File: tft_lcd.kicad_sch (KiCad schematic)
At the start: 4 parts, among them J1 Left_02x24, J2 Right Header, J3 Right_02x24, J4 Left Header

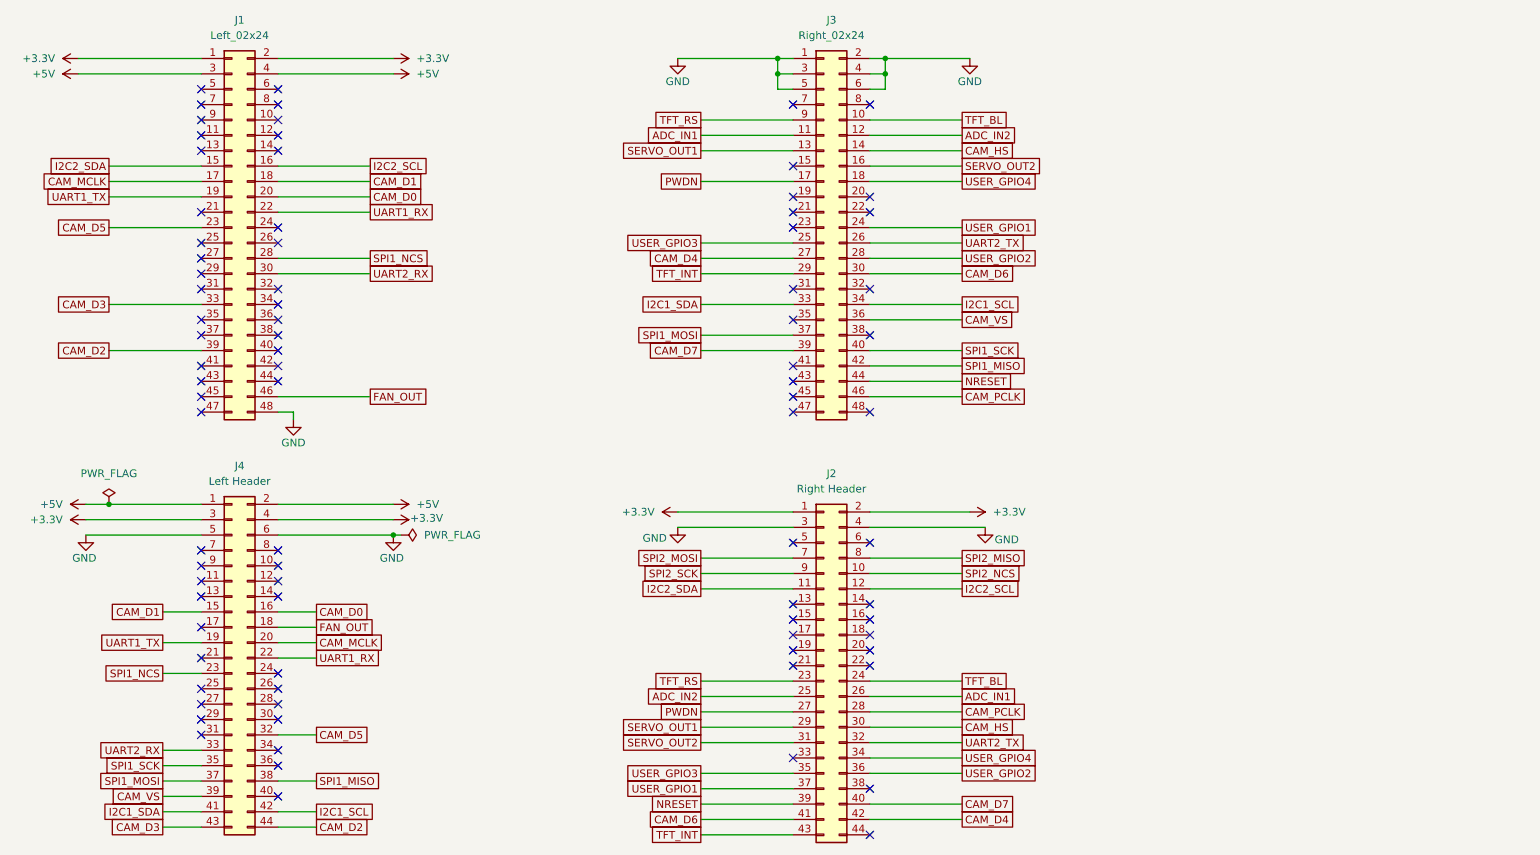
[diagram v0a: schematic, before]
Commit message: completed part placement
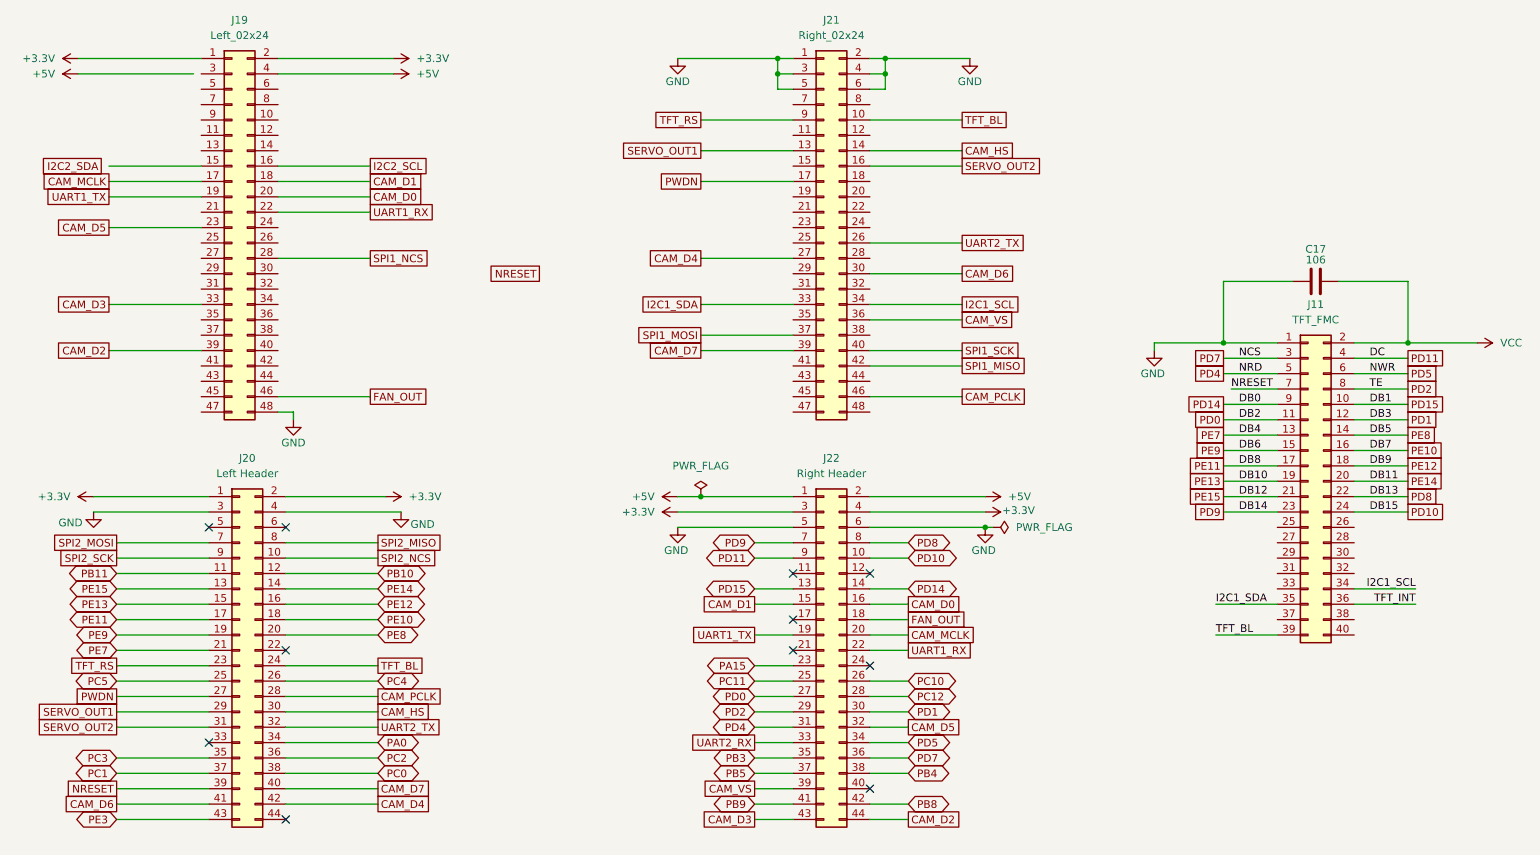
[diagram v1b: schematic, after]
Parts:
- added C17: 106, Capacitor_SMD:C_0805_2012Metric_Pad1.18x1.45mm_HandSolder, symbol LM2676S-3.3_NOPB:C
- added J11: TFT_FMC, Connector_PinHeader_2.54mm:PinHeader_2x20_P2.54mm_Vertical, symbol LM2676S-3.3_NOPB:Conn_02x20_Odd_Even
- J19: renamed from J1; footprint Connector_PinHeader_2.54mm:PinHeader_2x24_P2.54mm_Vertical -> (none)
- J20: renamed from J2; value Right Header -> Left Header
- J21: renamed from J3; footprint Connector_PinHeader_2.54mm:PinHeader_2x24_P2.54mm_Vertical -> (none)
- J22: renamed from J4; value Left Header -> Right Header
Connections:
- net +5V: no longer J19.3 (Pin_3)
- net GND: now also C17.1, J11.1 (Pin_1)
- net I2C1_SCL: now also J11.34 (Pin_34); no longer J22.42 (Pin_42)
- net I2C1_SDA: now also J11.35 (Pin_35); no longer J22.41 (Pin_41)
- net I2C2_SCL: no longer J20.12 (Pin_12)
- net I2C2_SDA: no longer J19.15 (Pin_15), J20.11 (Pin_11)
- net NRESET: now also J11.7 (Pin_7); no longer J21.44 (Pin_44)
- net SPI1_MISO: no longer J22.38 (Pin_38)
- net SPI1_MOSI: no longer J22.37 (Pin_37)
- net SPI1_NCS: no longer J22.23 (Pin_23)
- net SPI1_SCK: no longer J22.35 (Pin_35)
- net TFT_BL: now also J11.39 (Pin_39)
- net TFT_INT: now also J11.36 (Pin_36); no longer J20.43 (Pin_43), J21.29 (Pin_29)
- net UART2_RX: no longer J19.30 (Pin_30)
- net PD10: now reaches J22.10 (Pin_10)
- net PD10: now also J11.24 (Pin_24)
- net PD15: now reaches J22.13 (Pin_13)
- net PD15: now also J11.10 (Pin_10)
- net PD14: now reaches J22.14 (Pin_14)
- net PD14: now also J11.9 (Pin_9)
- net PC11: now reaches J22.25 (Pin_25)
- net PC10: now reaches J22.26 (Pin_26)
- net PD0: now reaches J22.27 (Pin_27)
- net PD0: now also J11.11 (Pin_11)
- net PC12: now reaches J22.28 (Pin_28)
- net PD2: now reaches J22.29 (Pin_29)
- net PD2: now also J11.8 (Pin_8)
- net PD1: now reaches J22.30 (Pin_30)
- net PD1: now also J11.12 (Pin_12)
- net PD4: now reaches J22.31 (Pin_31)
- net PD4: now also J11.5 (Pin_5)
- net PD5: now reaches J22.34 (Pin_34)
- net PD5: now also J11.6 (Pin_6)
- net PD7: now reaches J22.36 (Pin_36)
- net PD7: now also J11.3 (Pin_3)
- net PD9: now reaches J22.7 (Pin_7)
- net PD9: now also J11.23 (Pin_23)
- net PD8: now reaches J22.8 (Pin_8)
- net PD8: now also J11.22 (Pin_22)
- net PD11: now reaches J22.9 (Pin_9)
- net PD11: now also J11.4 (Pin_4)
- net PE15: now reaches J20.13 (Pin_13)
- net PE15: now also J11.21 (Pin_21)
- net PE14: now reaches J20.14 (Pin_14)
- net PE14: now also J11.20 (Pin_20)
- net PE13: now reaches J20.15 (Pin_15)
- net PE13: now also J11.19 (Pin_19)
- net PE12: now reaches J20.16 (Pin_16)
- net PE12: now also J11.18 (Pin_18)
- net PE11: now reaches J20.17 (Pin_17)
- net PE11: now also J11.17 (Pin_17)
- net PE10: now reaches J20.18 (Pin_18)
- net PE10: now also J11.16 (Pin_16)
- net PE9: now reaches J20.19 (Pin_19)
- net PE9: now also J11.15 (Pin_15)
- net PE8: now reaches J20.20 (Pin_20)
- net PE8: now also J11.14 (Pin_14)
- net PE7: now reaches J20.21 (Pin_21)
- net PE7: now also J11.13 (Pin_13)
- net PC0: now reaches J20.38 (Pin_38)
- net ADC_IN1: no longer names the net of J21.11 (Pin_11)
- net ADC_IN1: no longer J20.26 (Pin_26)
- net ADC_IN2: no longer names the net of J21.12 (Pin_12)
- net ADC_IN2: no longer J20.25 (Pin_25)
- net USER_GPIO1: no longer names the net of J21.24 (Pin_24)
- net USER_GPIO1: no longer J20.37 (Pin_37)
- net USER_GPIO2: no longer names the net of J21.28 (Pin_28)
- net USER_GPIO2: no longer J20.36 (Pin_36)
- net USER_GPIO3: no longer names the net of J21.25 (Pin_25)
- net USER_GPIO3: no longer J20.35 (Pin_35)
- net USER_GPIO4: no longer names the net of J21.18 (Pin_18)
- net USER_GPIO4: no longer J20.34 (Pin_34)
- new net PA0: J20.34 (Pin_34)
- new net PA15: J22.23 (Pin_23)
- new net PB10: J20.12 (Pin_12)
- new net PB11: J20.11 (Pin_11)
- new net PB3: J22.35 (Pin_35)
- new net PB4: J22.38 (Pin_38)
- new net PB5: J22.37 (Pin_37)
- new net PB8: J22.42 (Pin_42)
- new net PB9: J22.41 (Pin_41)
- new net PC1: J20.37 (Pin_37)
- new net PC2: J20.36 (Pin_36)
- new net PC3: J20.35 (Pin_35)
- new net PC4: J20.26 (Pin_26)
- new net PC5: J20.25 (Pin_25)
- new net PE3: J20.43 (Pin_43)
- new net VCC: C17.2, J11.2 (Pin_2)
- no-connect marks 83 -> 11
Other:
- moved on the sheet: J20, J22
